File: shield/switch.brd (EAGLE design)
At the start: 19.7 x 15.2 mm, 4 parts

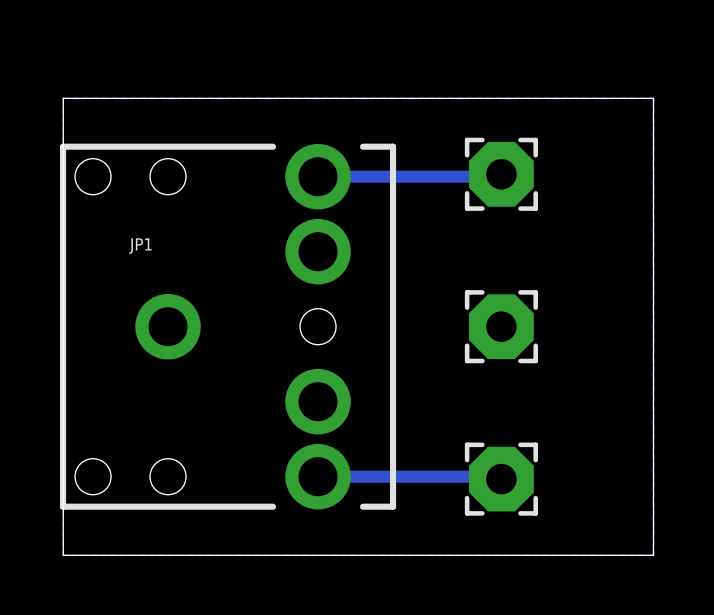
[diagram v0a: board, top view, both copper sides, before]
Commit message: fix ground plane routing on switch mount board
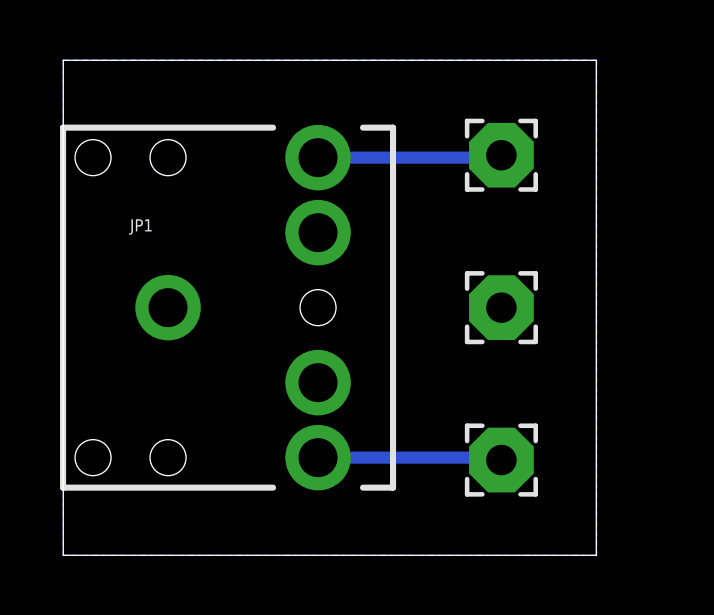
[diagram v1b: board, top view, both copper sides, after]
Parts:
- moved LT 0.64 mm to (14.6, 13.3)
- moved GND 0.64 mm to (14.6, 8.26)
- moved JP1 0.64 mm to (3.49, 8.26)
- moved SW 0.63 mm to (14.6, 3.17)
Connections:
- removed net N$3: GND.1, JP1.SLEEVE
- new net GND: GND.1, JP1.SLEEVE
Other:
- board size 19.7 x 15.2 mm -> 17.8 x 16.5 mm
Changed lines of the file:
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@@
 <board>
 <plain>
-<wire x1="0" y1="0" x2="19.6725" y2="0" width="0" layer="20"/>
-<wire x1="19.6725" y1="0" x2="19.6725" y2="15.23" width="0" layer="20"/>
-<wire x1="19.6725" y1="15.23" x2="0" y2="15.23" width="0" layer="20"/>
-<wire x1="0" y1="15.23" x2="0" y2="0" width="0" layer="20"/>
+<wire x1="0" y1="0" x2="17.7675" y2="0" width="0" layer="20"/>
+<wire x1="17.7675" y1="0" x2="17.7675" y2="16.5" width="0" layer="20"/>
+<wire x1="17.7675" y1="16.5" x2="0" y2="16.5" width="0" layer="20"/>
+<wire x1="0" y1="16.5" x2="0" y2="0" width="0" layer="20"/>
 </plain>
 <attributes>
@@
 </variantdefs>
 <classes>
-<class number="0" name="default" width="0" drill="0">
+<class number="0" name="default" width="0.3048" drill="0.508">
+<clearance class="0" value="0.254"/>
 </class>
 </classes>
@@
 </autorouter>
 <elements>
-<element name="JP1" library="SparkFun-Connectors" package="AUDIO-JACK" value="" x="3.4925" y="7.62"/>
-<element name="SW" library="wirepad" package="2,15/1,0" value="" x="14.605" y="2.54" smashed="yes">
-<attribute name="VALUE" x="14.605" y="3.54" size="0.0254" layer="27"/>
+<element name="JP1" library="SparkFun-Connectors" package="AUDIO-JACK" value="" x="3.4925" y="8.255"/>
+<element name="SW" library="wirepad" package="2,15/1,0" value="" x="14.605" y="3.175" smashed="yes">
+<attribute name="VALUE" x="14.605" y="4.175" size="0.0254" layer="27"/>
 </element>
-<element name="LT" library="wirepad" package="2,15/1,0" value="" x="14.605" y="12.7" smashed="yes">
-<attribute name="VALUE" x="14.605" y="13.7" size="0.0254" layer="27"/>
+<element name="LT" library="wirepad" package="2,15/1,0" value="" x="14.605" y="13.335" smashed="yes">
+<attribute name="VALUE" x="14.605" y="14.335" size="0.0254" layer="27"/>
 </element>
-<element name="GND" library="wirepad" package="2,15/1,0" value="" x="14.605" y="7.62" smashed="yes">
-<attribute name="VALUE" x="14.605" y="8.62" size="0.0254" layer="27"/>
+<element name="GND" library="wirepad" package="2,15/1,0" value="" x="14.605" y="8.255" smashed="yes">
+<attribute name="VALUE" x="14.605" y="9.255" size="0.0254" layer="27"/>
 </element>
 </elements>
@@
 <contactref element="JP1" pad="RING"/>
 <contactref element="LT" pad="1"/>
-<wire x1="8.4925" y1="12.62" x2="14.605" y2="12.62" width="0.4064" layer="16"/>
-<wire x1="14.605" y1="12.62" x2="14.605" y2="12.7" width="0.4064" layer="16"/>
+<wire x1="8.4925" y1="13.255" x2="14.605" y2="13.255" width="0.4064" layer="16"/>
+<wire x1="14.605" y1="13.255" x2="14.605" y2="13.335" width="0.4064" layer="16"/>
 </signal>
 <signal name="N$2">
 <contactref element="JP1" pad="TIP"/>
 <contactref element="SW" pad="1"/>
-<wire x1="8.4925" y1="2.62" x2="14.605" y2="2.62" width="0.4064" layer="16"/>
-<wire x1="14.605" y1="2.62" x2="14.605" y2="2.54" width="0.4064" layer="16"/>
+<wire x1="8.4925" y1="3.255" x2="14.605" y2="3.255" width="0.4064" layer="16"/>
+<wire x1="14.605" y1="3.255" x2="14.605" y2="3.175" width="0.4064" layer="16"/>
 </signal>
-<signal name="N$3">
+<signal name="GND">
 <contactref element="JP1" pad="SLEEVE"/>
 <contactref element="GND" pad="1"/>
-<wire x1="3.4925" y1="7.62" x2="14.605" y2="7.62" width="0" layer="19" extent="1-1"/>
-</signal>
-<signal name="GND">
 <polygon width="0.4064" layer="16">
-<vertex x="0" y="15.24"/>
-<vertex x="19.685" y="15.24"/>
-<vertex x="19.685" y="0"/>
+<vertex x="0" y="16.51"/>
+<vertex x="17.78" y="16.51"/>
+<vertex x="17.78" y="0"/>
 <vertex x="0" y="0"/>
 </polygon>
